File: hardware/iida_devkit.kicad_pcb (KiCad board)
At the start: 4 copper layers, 160 parts, among them J1 B2B-PH-K-S, J10 PRPC001DAAN-RC, J11 PRPC006SAAN-RC, J12 PRPC004SAAN-RC, J13 PRPC001DAAN-RC, J14 PRPC006SAAN-RC, J15 G85D1160022HHR, J2 USB4110-GF-A, J3 PRPC001DAAN-RC, J4 PRPC001DAAN-RC, J5 PRPC001DAAN-RC, J6 PRPC001DAAN-RC, J7 PRPC001DAAN-RC, J8 SBH11-NBPC-D05-SM-BK, J9 PRPC006SAAN-RC, Q1 IRLML2246TRPBF, Q2 DMN2046U-7, Q3 DMN2046U-7, Q4 IRLML2246TRPBF, Q5 IRLML2246TRPBF, Q6 MMBT3904, U1 USBLC6-2SC6, U10 SARA-R500S-61B, U2 S-8240ADQ-M6T1U, U3 MCP73811T-420I-OT, U4 TPS62A01PDDCR, U5 AT25SF081B-SSHD-B, U6 MCP9808, U7 STM32L552CETx, U8 74AVC1T45DW-7, U9 74AVC1T45DW-7, Y1 ABS05-32.768KHZ-9-T, Y2 ECS-160-9-37-CKM-TR3

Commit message: HW: Layout modem and SIM together
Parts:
- moved FID2 186.3 mm to (25.1, 177.1)
- moved FID3 186.3 mm to (25.1, 180.7)
- moved H1 186.3 mm to (20.4, 174.8)
- moved H2 186.3 mm to (20.4, 180.7)
- moved H3 186.3 mm to (20.4, 186.7)
- moved H4 186.3 mm to (20.4, 192.6)
- moved FID1 186.3 mm to (25.1, 173.6)
- moved TP1 183.0 mm to (31.0, 181.2)
- moved TP2 183.0 mm to (31.0, 184.8)
- moved TP3 183.0 mm to (31.0, 188.3)
- moved TP4 183.0 mm to (31.0, 191.8)
- moved TP5 183.0 mm to (34.5, 181.2)
- moved TP6 183.0 mm to (34.5, 184.8)
- moved TP7 183.0 mm to (34.5, 188.3)
- moved LED1 125.2 mm to (68.8, 31.7), turned to 90 degrees
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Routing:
- net /Modem/VSIM: track 0.00 -> 37.7 mm, vias 0 -> 2
- net /Modem/SIM_CLK: track 0.00 -> 30.3 mm, vias 0 -> 2
- net /Modem/SIM_IO: track 0.00 -> 20.1 mm, vias 0 -> 3
- net /Modem/MODEM_RX_1.8V: track 0.00 -> 17.8 mm
- net /Modem/SIM_RST: track 0.00 -> 17.2 mm
- net /Modem/MODEM_TX_1.8V: track 0.00 -> 16.2 mm
- net /Modem/NET_IND: track 0.00 -> 8.20 mm, vias 0 -> 2
- net /Modem/~{RESET}: track 0.00 -> 6.09 mm
- net GND: track 19.0 -> 24.8 mm, vias 43 -> 76
- net /MCU/~{MODEM_RESET}: track 0.00 -> 4.60 mm, vias 0 -> 1
- net /Modem/RTS: track 0.00 -> 4.42 mm
- net /Modem/DTR: track 0.00 -> 4.05 mm
- net /Antenna/ANT: track 3.80 -> 0.00 mm
- net +3.3V: track 0.00 -> 3.05 mm, vias 0 -> 7
- net /Modem/V_INT: track 0.00 -> 1.75 mm, vias 0 -> 3
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- added copper zone on F.Cu, net +3.3V
- added copper zone on F.Cu, net /MCU/~{MODEM_PWR_EN}
- added copper zone on F.Cu, net /Modem/+3.3V_MDM
- added copper zone on F.Cu, net /Modem/+3.3V_MDM_UNFILTERED
- added copper zone on F.Cu, net /Modem/NET_IND
- added copper zone on F.Cu, net /Modem/V_INT
- added copper zone on F.Cu, net Net-(J13-Pin_2)
- added copper zone on F.Cu, net Net-(J7-Pin_2)
- added copper zone on F.Cu, net Net-(LED1-K)
- added copper zone on F.Cu, net Net-(LED5-K)
- added copper zone on F.Cu, net Net-(Q5-G)
- added copper zone on F.Cu, net Net-(Q6-B)
- added copper zone on F.Cu, net Net-(Q6-C)
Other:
- board text added: "+3.3V"
- board text added: "+BATT>"
- board text added: "-BATT>"
- board text added: "<+3.3V"
- board text added: "<GND"
- board text added: "<V_{BAT}"
- board text added: "EXT+5V>"
- board text added: "IDD"
- board text added: "NET IND"

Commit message: HW: Layout MCU section
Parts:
- D1, D2, D3, D4, D5: value CDBA140LL-HF -> CDBA240LL-HF
- TVS10, TVS11, TVS2, TVS3, TVS4, TVS5, TVS6, TVS7, TVS8, TVS9: value SMAJ6.0CA-13-F -> CPDUC5V0USP-HF; footprint Diode_SMD:D_SMA_Handsoldering -> Diode_SMD:D_0603_1608Metric_Pad1.05x0.95mm_HandSolder
- U2: footprint Package_TO_SOT_SMD:SOT-23-6_Handsoldering -> Package_TO_SOT_SMD:SOT-23-6
- moved C26 72.7 mm to (244.7, 68.8)
- moved C28 72.7 mm to (244.7, 67.2)
- moved C34 72.7 mm to (233.4, 66.9)
- moved C35 72.7 mm to (227.9, 64.9)
- moved FB3 72.7 mm to (245.6, 61.5)
- moved J15 72.7 mm to (230.6, 80.5)
- moved LED5 72.7 mm to (217.2, 35.2)
- moved Q5 72.7 mm to (247.5, 73.2)
- moved R27 72.7 mm to (249.7, 75.8)
- moved R28 72.7 mm to (246.3, 75.8)
- moved R29 72.7 mm to (225.9, 38.2)
- moved R30 72.7 mm to (224.3, 38.2)
- moved R34 72.7 mm to (237.9, 39.5)
- moved R35 72.7 mm to (235.9, 39.5)
- moved R36 72.7 mm to (227.9, 37.5)
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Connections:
- J11 pad 4: /MCU/MODEM_TX -> /MCU/MODEM_RX
- J11 pad 5: /MCU/MODEM_RX -> /MCU/MODEM_TX
- J12 pad 2: /MCU/I2C_SCL -> /MCU/I2C_SDA
- J12 pad 3: /MCU/I2C_SDA -> /MCU/I2C_SCL
- J9 pad 4: /MCU/COM_UART_TX -> /MCU/COM_UART_RX
- J9 pad 5: /MCU/COM_UART_RX -> /MCU/COM_UART_TX
- TVS2 pad 1: /MCU/COM_UART_RX -> /MCU/COM_UART_TX
- TVS3 pad 1: /MCU/MODEM_RX -> /MCU/MODEM_TX
- TVS4 pad 1: /MCU/I2C_SDA -> /MCU/I2C_SCL
- TVS5 pad 1: /MCU/COM_UART_TX -> /MCU/COM_UART_RX
- TVS6 pad 1: /MCU/MODEM_TX -> /MCU/MODEM_RX
- TVS7 pad 1: /MCU/I2C_SCL -> /MCU/I2C_SDA
- U2 pad 4: (no net) -> unconnected-(U2-NC-Pad4)
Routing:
- net /MCU/~{RESET}: track 0.00 -> 47.1 mm, vias 0 -> 2
- net /MCU/SWDIO: track 0.00 -> 47.1 mm, vias 0 -> 4
- net GND: track 24.8 -> 69.2 mm, vias 76 -> 184
- net /MCU/SWCLK: track 0.00 -> 42.8 mm, vias 0 -> 2
- net /MCU/SWO: track 0.00 -> 38.3 mm, vias 0 -> 2
- net /MCU/I2C_SCL: track 0.00 -> 37.2 mm, vias 0 -> 2
- net /MCU/I2C_SDA: track 0.00 -> 34.6 mm
- net +3.3V: track 3.05 -> 36.2 mm, vias 7 -> 45
- net /MCU/HWID_2: track 0.00 -> 31.6 mm, vias 0 -> 2
- net /MCU/HWID_1: track 0.00 -> 28.2 mm, vias 0 -> 2
- net /MCU/MODEM_RX: track 1.27 -> 28.4 mm
- net /MCU/LED_A: track 0.00 -> 26.7 mm, vias 0 -> 2
- net /MCU/MODEM_TX: track 1.27 -> 27.2 mm, vias 1 -> 3
- net /MCU/LED_B: track 0.00 -> 24.2 mm, vias 0 -> 2
- net /MCU/DBG_GPIO: track 0.00 -> 22.8 mm, vias 0 -> 2
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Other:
- board text added: "+3.3V>"
- board text added: "<COM RX"
- board text added: "<COM TX"
- board text added: "<GPIO"
- board text added: "<SCL"
- board text added: "<SDA"
- board text added: "A"
- board text added: "B"
- board text added: "C"
- board text added: "GND>"
- board text added: "Hardware ID"
- board text added: "MODEM RX>"
- board text added: "MODEM TX>"
- board text added: "RESET"

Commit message: HW: Cleanup layout
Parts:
- moved J5 14.3 mm to (67.9, 50.0)
- moved J6 13.6 mm to (59.0, 50.0)
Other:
- board text added: "V_{BAT}>"
- board text removed: "<V_{BAT}"
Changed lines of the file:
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@@
 			(at 0 -1.65 90)
 			(layer "F.SilkS")
+			(hide yes)
 			(effects
 				(font
@@
 		(tags "Through hole pin header THT 1x06 2.54mm single row")
 		(property "Reference" "J14"
-			(at 0 -2.33 90)
+			(at -0.0875 -3.17 180)
 			(layer "F.SilkS")
 			(effects
@@
 			(at 0.2 2.2875 180)
 			(layer "F.SilkS")
+			(hide yes)
 			(effects
 				(font
@@
 			(at -4.2 0 90)
 			(layer "F.SilkS")
+			(hide yes)
 			(effects
 				(font
@@
 			(at 0 -1.43 90)
 			(layer "F.SilkS")
+			(hide yes)
 			(effects
 				(font
@@
 			(at -4.2 0 90)
 			(layer "F.SilkS")
+			(hide yes)
 			(effects
 				(font
@@
 			(at 0 -3.4 90)
 			(layer "F.SilkS")
+			(hide yes)
 			(effects
 				(font
@@
 			(at 0 2.2 0)
 			(layer "F.SilkS")
+			(hide yes)
 			(effects
 				(font
@@
 		(tags "resistor handsolder")
 		(property "Reference" "FB3"
-			(at 0.1125 -1.5375 90)
+			(at -0.0875 -2.25 180)
 			(layer "F.SilkS")
 			(effects
@@
 			(at -2.6 0 0)
 			(layer "F.SilkS")
+			(hide yes)
 			(effects
 				(font
@@
 			(at 0 -2.2 0)
 			(layer "F.SilkS")
+			(hide yes)
 			(effects
 				(font
@@
 			(at 5.6 0 0)
 			(layer "F.SilkS")
+			(hide yes)
 			(effects
 				(font
@@
 		(tags "solder jumper open")
 		(property "Reference" "JP1"
-			(at 0 -2 90)
+			(at 3.7 0 180)
 			(layer "F.SilkS")
 			(effects
@@
 			(at 4.1375 0 0)
 			(layer "F.SilkS")
+			(hide yes)
 			(effects
 				(font
@@
 		(tags "Surface mounted pin header SMD 2x05 2.54mm double row")
 		(property "Reference" "J8"
-			(at 0 -7.41 90)
+			(at -5.275 -7.32 180)
 			(layer "F.SilkS")
 			(effects
@@
 			(at -4.3 0.05 90)
 			(layer "F.SilkS")
+			(hide yes)
 			(effects
 				(font
@@
 			(at 0 -1.4 0)
 			(layer "F.SilkS")
+			(hide yes)
 			(effects
 				(font
@@
 			(at 0 1.4 0)
 			(layer "F.SilkS")
+			(hide yes)
 			(effects
 				(font
@@
 			(at -3 0 0)
 			(layer "F.SilkS")
+			(hide yes)
 			(effects
 				(font
@@
 			(at 4.725 0 0)
 			(layer "F.SilkS")
+			(hide yes)
 			(effects
 				(font
@@
 			(at 3 0 0)
 			(layer "F.SilkS")
+			(hide yes)
 			(effects
 				(font
@@
 			(at 3.2 0 90)
 			(layer "F.SilkS")
+			(hide yes)
 			(effects
 				(font
@@
 	(footprint "Connector_PinHeader_2.54mm:PinHeader_1x02_P2.54mm_Vertical"
 		(layer "F.Cu")
-		(at 65.925 61.75 90)
+		(at 59 50 90)
 		(descr "Through hole straight pin header, 1x02, 2.54mm pitch, single row")
 		(tags "Through hole pin header THT 1x02 2.54mm single row")
 		(property "Reference" "J6"
-			(at 0 -2.33 90)
+			(at 2.4 1.2 180)
 			(layer "F.SilkS")
 			(effects
@@
 			(unlocked yes)
 			(layer "F.SilkS")
+			(hide yes)
 			(effects
 				(font
@@
 			(at 0 2.2 0)
 			(layer "F.SilkS")
+			(hide yes)
 			(effects
 				(font
@@
 			(at 0 -2.2 0)
 			(layer "F.SilkS")
+			(hide yes)
 			(effects
 				(font
@@
 	(footprint "Connector_PinHeader_2.54mm:PinHeader_1x02_P2.54mm_Vertical"
 		(layer "F.Cu")
-		(at 59.875 61.75 -90)
+		(at 67.94 50 -90)
 		(descr "Through hole straight pin header, 1x02, 2.54mm pitch, single row")
 		(tags "Through hole pin header THT 1x02 2.54mm single row")
 		(property "Reference" "J5"
-			(at 0 -2.33 90)
+			(at -2.4 1.275 180)
 			(layer "F.SilkS")
 			(effects
@@
 			(at 4.925 0 0)
 			(layer "F.SilkS")
+			(hide yes)
 			(effects
 				(font
@@
 			(at 4.1375 0 0)
 			(layer "F.SilkS")
+			(hide yes)
 			(effects
 				(font
@@
 			(at 4 0 0)
 			(layer "F.SilkS")
+			(hide yes)
 			(effects
 				(font
@@
 			(at 7 0.2 0)
 			(layer "F.SilkS")
+			(hide yes)
 			(effects
 				(font
@@
 		(tags "SC-59 hand-soldering")
 		(property "Reference" "Q6"
-			(at 3.8 0 -90)
+			(at 3.625 0 0)
 			(layer "F.SilkS")
 			(effects
@@
 			(at 3.4 0 90)
 			(layer "F.SilkS")
+			(hide yes)
 			(effects
 				(font
@@
 			(at 3.3 0 90)
 			(layer "F.SilkS")
+			(hide yes)
 			(effects
 				(font
@@
 			(at 5.725 0 0)
 			(layer "F.SilkS")
+			(hide yes)
 			(effects
 				(font
@@
 			(at 3.2 0 90)
 			(layer "F.SilkS")
+			(hide yes)
 			(effects
 				(font
@@
 			(at 4.925 0 0)
 			(layer "F.SilkS")
+			(hide yes)
 			(effects
 				(font
@@
 			(at -3.2 0 90)
 			(layer "F.SilkS")
+			(hide yes)
 			(effects
 				(font
@@
 		(tags "Through hole pin header THT 1x02 2.54mm single row")
 		(property "Reference" "J4"
-			(at 0 5.2 0)
+			(at -2.6 2.875 0)
 			(layer "F.SilkS")
 			(effects
@@
 		)
 	)
-	(gr_text "<GND"
-		(at 58.4 59.95 90)
+	(gr_text "GND>"
+		(at 64 51.85 90)
 		(layer "F.SilkS" knockout)
 		(effects
@@
 				(thickness 0.15)
 			)
-			(justify left bottom)
+			(justify right top)
 		)
 	)
@@
 		)
 	)
-	(gr_text "<GND"
-		(at 69.8 59.95 90)
+	(gr_text "GND>"
+		(at 60.475 51.85 90)
 		(layer "F.SilkS" knockout)
 		(effects
@@
 				(thickness 0.15)
 			)
-			(justify left bottom)
+			(justify right top)
 		)
 	)
@@
 		)
 	)
-	(gr_text "<+3.3V"
-		(at 61.2 59.95 90)
+	(gr_text "+3.3V>"
+		(at 66.8 51.8 90)
 		(layer "F.SilkS" knockout)
 		(effects
@@
 				(thickness 0.15)
 			)
-			(justify left bottom)
+			(justify right top)
 		)
 	)
@@
 	)
 	(gr_text "IDD"
-		(at 64.4 46.75 90)
+		(at 61.6 44.8 0)
 		(layer "F.SilkS" knockout)
 		(effects
@@
 		)
 	)
-	(gr_text "<V_{BAT}"
-		(at 66.8 59.95 90)
+	(gr_text "V_{BAT}>"
+		(at 57.475 51.85 90)
 		(layer "F.SilkS" knockout)
 		(effects
@@
 				(thickness 0.15)
 			)
-			(justify left bottom)
+			(justify right top)
 		)
 	)
@@
 			(pts
 				(xy 57.3375 40.2) (xy 58.8 41.4) (xy 58.8 43.4) (xy 61.2 43.4) (xy 61.2 41.4) (xy 62 40.2) (xy 62 38.4)
-				(xy 64 38.4) (xy 64 34.4) (xy 62.5375 34.4) (xy 62.5375 35.8) (xy 60.2 35.8) (xy 60.2 38.4) (xy 57.3375 38.4)
+				(xy 64 38.4) (xy 64 34.4) (xy 62.5375 34.4) (xy 62.5375 37.2) (xy 60.8 37.2) (xy 60.8 38.4) (xy 57.3375 38.4)
 			)
 		)

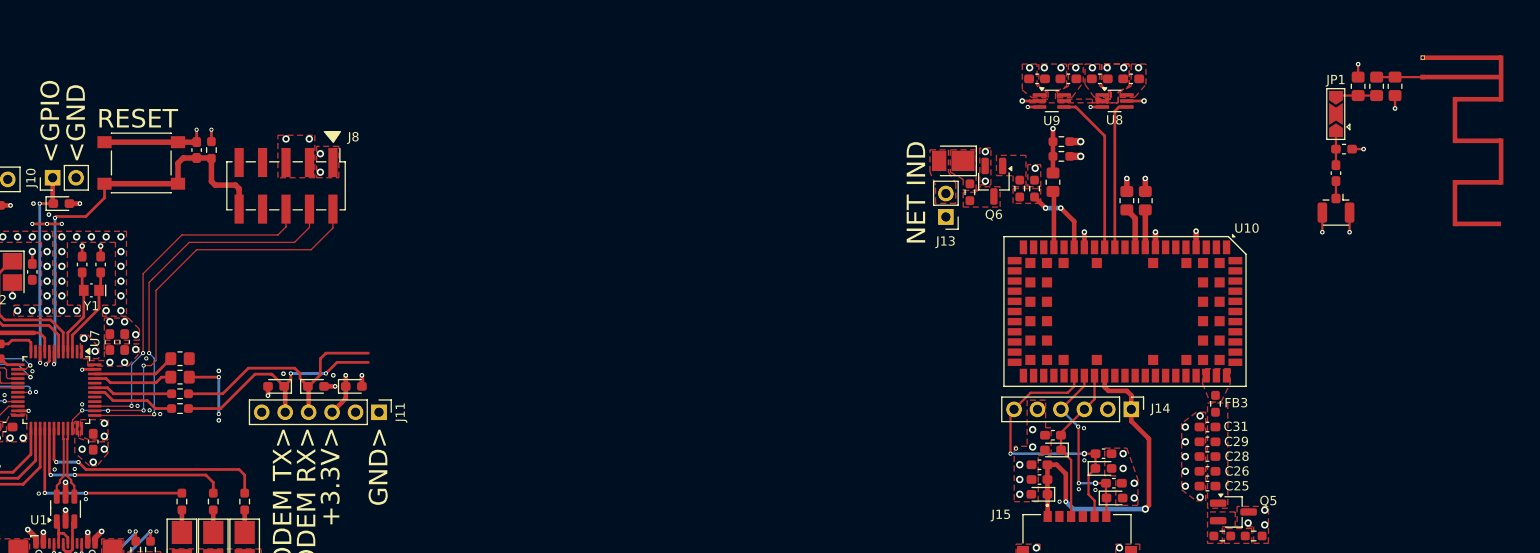
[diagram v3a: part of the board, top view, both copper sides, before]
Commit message: HW: Refine modem layout
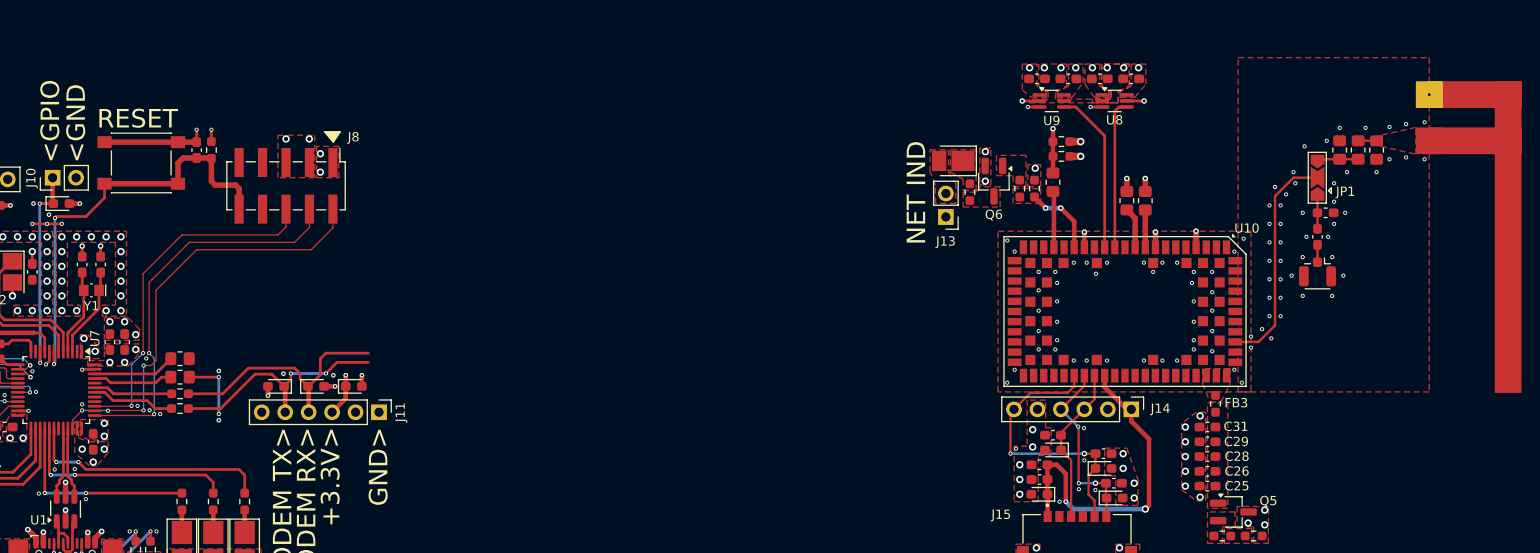
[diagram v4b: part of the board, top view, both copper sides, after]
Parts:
- moved AE1 7.18 mm to (256.6, 47.2)
- moved C38 7.18 mm to (256.6, 43.4)
- moved JP1 7.18 mm to (256.6, 37.0)
- moved L2 7.18 mm to (257.5, 40.8)
- moved R37 7.18 mm to (259.0, 34.0)
- moved R38 7.18 mm to (261.0, 34.0)
- moved R39 7.18 mm to (263.0, 34.0)
- moved AE2 4.11 mm to (268.7, 28.0)
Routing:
- net /Antenna/ANT: track 0.00 -> 24.5 mm
- net GND: track 69.2 -> 60.9 mm, vias 184 -> 270
- net /Antenna/ANT_PCB: track 5.00 -> 2.00 mm
- net /Modem/VSIM: track 37.7 -> 36.8 mm
- added copper zone on F.Cu, net /Antenna/ANT_PCB

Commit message: HW: Route sections together
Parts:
- moved TP3 259.6 mm to (241.0, 35.6), turned to 90 degrees
- moved TP4 258.9 mm to (241.4, 41.0), turned to 90 degrees
- moved TP1 256.3 mm to (245.6, 41.0)
- moved TP7 253.9 mm to (237.0, 35.0), turned to 90 degrees
- moved TP2 248.4 mm to (231.8, 38.6), turned to 90 degrees
- moved TP5 239.5 mm to (221.6, 31.6), turned to 90 degrees
- moved TP6 232.6 mm to (220.6, 45.2), turned to 90 degrees
- moved R2 85.5 mm to (119.7, 60.5), turned to 0 degrees
- moved Q1 83.8 mm to (117.1, 64.5), turned to 180 degrees
- moved J1 81.9 mm to (111.3, 61.0), turned to 180 degrees
- moved R5 81.7 mm to (124.9, 55.4), turned to 90 degrees
- moved Q3 81.6 mm to (134.9, 50.6)
- moved D3 81.3 mm to (112.5, 51.8), turned to -90 degrees
- moved C6 80.7 mm to (125.5, 49.7)
- moved C7 80.7 mm to (118.9, 48.0)
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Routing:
- net +VBAT: track 4.39 -> 84.4 mm, vias 5 -> 7
- net /MCU/~{MODEM_PWR_EN}: track 7.20 -> 66.2 mm
- net /MCU/~{MODEM_RESET}: track 4.60 -> 57.3 mm, vias 1 -> 2
- net /MCU/MODEM_TX: track 27.2 -> 68.9 mm, vias 3 -> 6
- net /MCU/MODEM_RX: track 28.4 -> 63.1 mm, vias 1 -> 2
- net /Modem/V_INT: track 1.75 -> 34.4 mm
- net Net-(J1-Pin_1): track 0.00 -> 11.4 mm
- net /MCU/SWDIO: track 47.1 -> 37.6 mm
- net /Modem/~{RESET}: track 6.09 -> 15.6 mm
- net /Modem/NET_IND: track 8.20 -> 17.4 mm
- net Net-(J1-Pin_2): track 30.3 -> 22.7 mm
- net /Modem/DTR: track 4.05 -> 10.2 mm
- net Net-(Q3-G): track 6.14 -> 0.00 mm
- net GND: track 60.9 -> 66.9 mm, vias 270 -> 279
- net /Modem/RTS: track 4.42 -> 10.3 mm
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- added copper zone on B.Cu, net +VBAT
- added copper zone on F.Cu, net Net-(Q3-G)
- added copper zone on B.Cu, net Net-(U1-VBUS)
- added copper zone on F.Cu, net Net-(U2-VM)
- removed copper zone on F.Cu, net Net-(J1-Pin_1)

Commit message: HW: Connect nets and fill layers
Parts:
- moved H4 228.0 mm to (214.4, 72.8)
- moved FID3 223.3 mm to (221.4, 74.2)
- moved H3 221.9 mm to (235.2, 131.2)
- moved FID1 211.1 mm to (231.0, 127.0)
- moved H2 124.3 mm to (81.6, 72.6)
- moved FID2 76.4 mm to (83.6, 128.0)
- moved H1 74.7 mm to (81.2, 131.4)
- moved C24 56.5 mm to (202.2, 73.6)
- moved C30 56.5 mm to (195.4, 73.6)
- moved C32 56.5 mm to (198.8, 73.6)
- moved C27 56.5 mm to (205.6, 73.6)
- moved U8 56.3 mm to (203.8, 75.8)
- moved U9 56.3 mm to (197.0, 75.8)
- moved U3 55.6 mm to (91.0, 95.7)
- moved C7 55.5 mm to (87.8, 94.0)
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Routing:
- net Net-(D2-K): track 0.00 -> 17.3 mm, vias 4 -> 2
- net +VBAT: track 84.4 -> 72.8 mm, vias 7 -> 6
- net +3.3V: track 36.7 -> 26.1 mm, vias 46 -> 39
- net /Modem/V_INT: track 34.4 -> 28.5 mm, vias 3 -> 2
- net /MCU/LED_C: track 21.8 -> 19.4 mm
- net /MCU/HSE_IN: track 16.3 -> 18.3 mm
- net /Antenna/ANT_PCB: track 2.00 -> 0.00 mm
- net /MCU/HSE_OUT: track 13.7 -> 15.7 mm
- net /MCU/LED_B: track 24.2 -> 22.8 mm
- net /MCU/LED_A: track 26.7 -> 25.3 mm
- net /Modem/MODEM_TX_1.8V: track 16.2 -> 15.1 mm
- net /MCU/MODEM_RX: track 63.1 -> 61.9 mm
- net /Modem/MODEM_RX_1.8V: track 17.8 -> 16.6 mm
- net GND: track 66.9 -> 65.9 mm, vias 279 -> 290
- net /MCU/MODEM_TX: track 68.9 -> 68.1 mm
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- added copper zone on B.Cu, net +3.3V
- added copper zone on B.Cu, net GND
- added copper zone on In1.Cu, net GND
- added copper zone on In2.Cu, net GND
- removed copper zone on B.Cu, net Net-(D2-K)
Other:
- board outline added: 180 x 64 mm

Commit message: HW: Cleanup layout
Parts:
- moved FID3 8.60 mm to (230.0, 74.0)
- moved FID1 1.00 mm to (230.0, 127.0)
- moved Q4 0.81 mm to (98.6, 95.6)
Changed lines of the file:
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@@
 	(footprint "Package_TO_SOT_SMD:SC-59_Handsoldering"
 		(layer "F.Cu")
-		(at 99.41 95.6 -90)
+		(at 98.6 95.6 -90)
 		(descr "SC-59, hand-soldering varaint, https://lib.chipdip.ru/images/import_diod/original/SOT-23_SC-59.jpg")
 		(tags "SC-59 hand-soldering")
 		(property "Reference" "Q4"
-			(at -3.05 -2.65 -90)
+			(at -1.4 -2.8 -90)
 			(layer "F.SilkS")
 			(effects
@@
 		(tags "connector JST PH side entry")
 		(property "Reference" "J1"
-			(at 1 4 0)
+			(at -1.465 3.85 0)
 			(layer "F.SilkS")
 			(effects
@@
 	(footprint "Fiducial:Fiducial_1mm_Mask2mm"
 		(layer "F.Cu")
-		(at 231 127)
+		(at 230 127)
 		(descr "Circular Fiducial, 1mm bare copper, 2mm soldermask opening (Level A)")
 		(tags "fiducial")
@@
 		(tags "Through hole pin header THT 1x02 2.54mm single row")
 		(property "Reference" "J3"
-			(at 2.4 0.8 90)
+			(at -2.2025 -2.6 180)
 			(layer "F.SilkS")
 			(effects
@@
 		(tags "SC-59 hand-soldering")
 		(property "Reference" "Q1"
-			(at 2 -1.35 0)
+			(at -1.265 -2.75 0)
 			(layer "F.SilkS")
 			(effects
@@
 		(tags "SOT TO_SOT_SMD")
 		(property "Reference" "U4"
-			(at 1.0625 -2.4 180)
+			(at -1.1975 -2.6 180)
 			(layer "F.SilkS")
 			(effects
@@
 	(footprint "Fiducial:Fiducial_1mm_Mask2mm"
 		(layer "F.Cu")
-		(at 221.4 74.2)
+		(at 230 74)
 		(descr "Circular Fiducial, 1mm bare copper, 2mm soldermask opening (Level A)")
 		(tags "fiducial")
@@
 		(tags "LQFP QFP")
 		(property "Reference" "U7"
-			(at -5.6 -4.2 90)
+			(at -4.2375 -4.46 90)
 			(layer "F.SilkS")
 			(effects
@@
 		(tags "SC-59 hand-soldering")
 		(property "Reference" "Q2"
-			(at 2.05 -1.275 -90)
+			(at -1.4 -2.74 -90)
 			(layer "F.SilkS")
 			(effects
@@
 	)
 	(via
-		(at 201.385337 77.135334)
+		(at 200.4 75.8)
 		(size 0.45)
 		(drill 0.25)
@@
 	)
 	(via
-		(at 98.2 97.6)
+		(at 97.39 97.6)
 		(size 0.8)
 		(drill 0.45)
@@
 	)
 	(via
-		(at 98.4 95.75)
+		(at 97.59 95.75)
 		(size 0.8)
 		(drill 0.45)
@@
 		(polygon
 			(pts
-				(xy 101.06 94.95) (xy 99.46 94.95) (xy 99.46 92.55) (xy 97.06 92.55) (xy 97.06 88.15) (xy 101.06 88.15)
+				(xy 101.06 94.95) (xy 98.66 94.95) (xy 98.66 92.55) (xy 97.06 92.55) (xy 97.06 88.15) (xy 101.06 88.15)
 			)
 		)
@@
 		(polygon
 			(pts
-				(xy 79.7475 91.6) (xy 79.7475 97.2) (xy 78.9475 98.2) (xy 76.9475 98.2) (xy 75.3475 99.4) (xy 73.1475 99.4)
-				(xy 73.1475 96.8) (xy 75.7975 96.8) (xy 75.7975 91.6)
+				(xy 79.8 91.6) (xy 79.8 98.2) (xy 76.9475 98.2) (xy 75.3475 99.4) (xy 73.1475 99.4) (xy 73.1475 96.8)
+				(xy 75.5975 96.8) (xy 75.5975 91.6)
 			)
 		)
@@
 		(polygon
 			(pts
-				(xy 101.021817 86.999851) (xy 96.8 87) (xy 96.8 92.8) (xy 99.26 92.8) (xy 99.26 94.95) (xy 95 94.95)
+				(xy 101.021817 86.999851) (xy 96.8 87) (xy 96.8 92.8) (xy 98.26 92.8) (xy 98.26 94.95) (xy 95 94.95)
 				(xy 95 84.6) (xy 101 84.6)
 			)
@@
 	)
 	(zone
+		(net 0)
+		(net_name "")
+		(layer "F.Cu")
+		(hatch edge 0.5)
+		(connect_pads
+			(clearance 0)
+		)
+		(min_thickness 0.125)
+		(filled_areas_thickness no)
+		(keepout
+			(tracks allowed)
+			(vias allowed)
+			(pads allowed)
+			(copperpour not_allowed)
+			(footprints allowed)
+		)
+		(fill
+			(thermal_gap 0.125)
+			(thermal_bridge_width 0.5)
+		)
+		(polygon
+			(pts
+				(xy 240 106.4) (xy 240 110.4) (xy 237.8 110.4) (xy 237.8 106.4)
+			)
+		)
+	)
+	(zone
 		(net 1)
 		(net_name "GND")
@@
 		(polygon
 			(pts
-				(xy 96.8 100) (xy 96.8 98.2) (xy 99.86 98.2) (xy 99.86 95.2) (xy 94.8 95.2) (xy 94.8 92.55) (xy 91.66 92.55)
+				(xy 96.8 100) (xy 96.8 98.2) (xy 99.26 98.2) (xy 99.26 95.2) (xy 94.8 95.2) (xy 94.8 92.55) (xy 91.66 92.55)
 				(xy 91.66 95.15) (xy 93.46 95.15) (xy 93.46 97.15) (xy 95.4 97.15) (xy 95.4 100)
 			)
@@
 		(polygon
 			(pts
-				(xy 109.735 103.45) (xy 97 103.45) (xy 97 95.25) (xy 98.8 95.25) (xy 98.8 101.65) (xy 109.735 101.65)
+				(xy 109.735 103.45) (xy 96.8 103.45) (xy 96.8 95.25) (xy 98.8 95.25) (xy 98.8 101.65) (xy 109.735 101.65)
 			)
 		)
